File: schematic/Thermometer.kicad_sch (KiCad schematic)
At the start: 17 parts, among them Q1 BC547, Q2 BC547, Q3 BC547, Q4 BC547, SW1 SW_SPDT, U1 CC56-12EWA, U2 DS18B20, U3 DS18B20

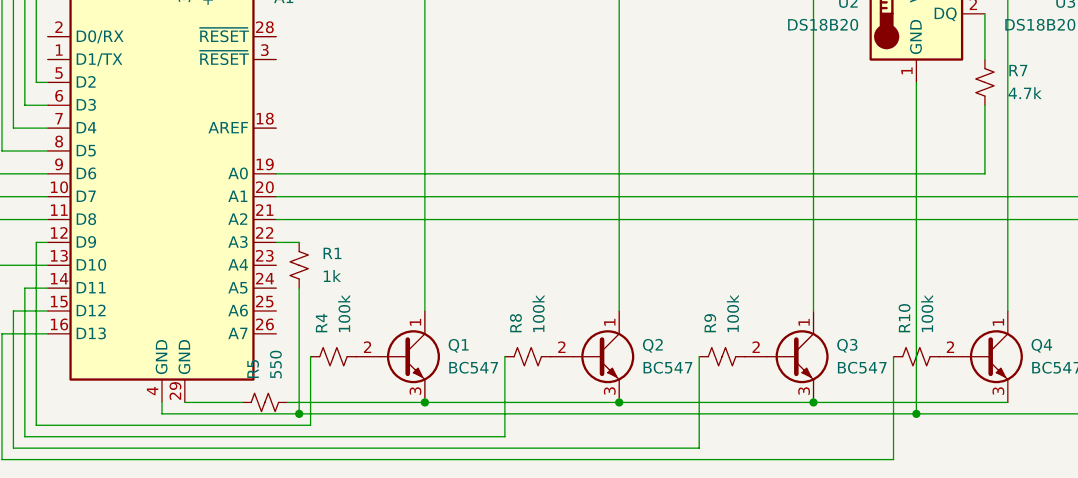
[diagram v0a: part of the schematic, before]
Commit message: Created a PCB design for the board
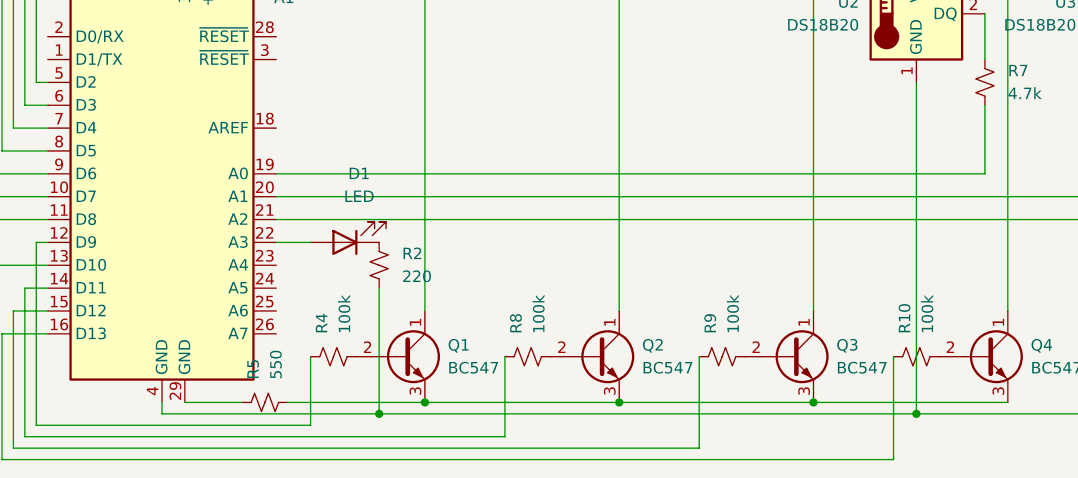
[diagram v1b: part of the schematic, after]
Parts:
- removed R1: 1k, symbol Device:R_Small_US
- added D1: LED, LED_THT:LED_D5.0mm, symbol Device:LED
- added R2: 220, Resistor_THT:R_Axial_DIN0204_L3.6mm_D1.6mm_P5.08mm_Horizontal, symbol Device:R_Small_US
- R10, R4, R5, R6, R7, R8, R9: footprint (none) -> Resistor_THT:R_Axial_DIN0204_L3.6mm_D1.6mm_P5.08mm_Horizontal
- SW1: footprint (none) -> Button_Switch_THT:SW_CK_JS202011CQN_DPDT_Straight
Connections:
- net at A1.4 (GND), SW1.3 (C), U2.1 (GND)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: now also R2.2
- net at A1.22 (A3): now also D1.2 (A)
- new net: D1.1 (K), R2.1
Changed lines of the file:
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@@
 	)
 	(junction
-		(at 54.61 95.25)
+		(at 63.5 95.25)
 		(diameter 0)
 		(color 0 0 0 0)
@@
 	(wire
 		(pts
-			(xy 52.07 76.2) (xy 54.61 76.2)
-		)
-		(stroke
-			(width 0)
-			(type default)
-		)
-	)
-	(wire
-		(pts
 			(xy 26.67 66.04) (xy 21.59 66.04)
 		)
@@
 	(wire
 		(pts
-			(xy 54.61 95.25) (xy 123.19 95.25)
+			(xy 63.5 95.25) (xy 123.19 95.25)
+		)
+		(stroke
+			(width 0)
+			(type default)
+		)
+	)
+	(wire
+		(pts
+			(xy 39.37 95.25) (xy 63.5 95.25)
 		)
 		(stroke
@@
 	(wire
 		(pts
+			(xy 52.07 76.2) (xy 55.88 76.2)
+		)
+		(stroke
+			(width 0)
+			(type default)
+		)
+	)
+	(wire
+		(pts
 			(xy 17.78 36.83) (xy 26.67 36.83)
 		)
@@
 	(wire
 		(pts
-			(xy 54.61 81.28) (xy 54.61 95.25)
-		)
-		(stroke
-			(width 0)
-			(type default)
-		)
-	)
-	(wire
-		(pts
-			(xy 39.37 95.25) (xy 54.61 95.25)
-		)
-		(stroke
-			(width 0)
-			(type default)
-		)
-	)
-	(wire
-		(pts
 			(xy 111.76 93.98) (xy 133.35 93.98)
 		)
@@
 		(pts
 			(xy 20.32 31.75) (xy 26.67 31.75)
+		)
+		(stroke
+			(width 0)
+			(type default)
+		)
+	)
+	(wire
+		(pts
+			(xy 63.5 81.28) (xy 63.5 95.25)
 		)
 		(stroke
@@
 			)
 		)
-		(property "Footprint" ""
+		(property "Footprint" "Resistor_THT:R_Axial_DIN0204_L3.6mm_D1.6mm_P5.08mm_Horizontal"
 			(at 80.01 88.9 0)
 			(effects
@@
 			)
 		)
-		(property "Footprint" ""
+		(property "Footprint" "Resistor_THT:R_Axial_DIN0204_L3.6mm_D1.6mm_P5.08mm_Horizontal"
 			(at 154.94 58.42 0)
 			(effects
@@
 			)
 		)
-		(property "Footprint" ""
+		(property "Footprint" "Resistor_THT:R_Axial_DIN0204_L3.6mm_D1.6mm_P5.08mm_Horizontal"
 			(at 130.81 58.42 0)
 			(effects
@@
 	(symbol
 		(lib_id "Device:R_Small_US")
+		(at 63.5 78.74 0)
+		(unit 1)
+		(exclude_from_sim no)
+		(in_bom yes)
+		(on_board yes)
+		(dnp no)
+		(fields_autoplaced yes)
+		(property "Reference" "R2"
+			(at 66.04 77.4699 0)
+			(effects
+				(font
+					(size 1.27 1.27)
+				)
+				(justify left)
+			)
+		)
+		(property "Value" "220"
+			(at 66.04 80.0099 0)
+			(effects
+				(font
+					(size 1.27 1.27)
+				)
+				(justify left)
+			)
+		)
+		(property "Footprint" "Resistor_THT:R_Axial_DIN0204_L3.6mm_D1.6mm_P5.08mm_Horizontal"
+			(at 63.5 78.74 0)
+			(effects
+				(font
+					(size 1.27 1.27)
+				)
+				(hide yes)
+			)
+		)
+		(property "Datasheet" "~"
+			(at 63.5 78.74 0)
+			(effects
+				(font
+					(size 1.27 1.27)
+				)
+				(hide yes)
+			)
+		)
+		(property "Description" "Resistor, small US symbol"
+			(at 63.5 78.74 0)
+			(effects
+				(font
+					(size 1.27 1.27)
+				)
+				(hide yes)
+			)
+		)
+		(pin "2"
+		)
+		(pin "1"
+		)
+		(instances
+			(project ""
+				(path "/81b9514e-2b12-47cb-ad97-5183a669bf2a"
+					(reference "R2")
+					(unit 1)
+				)
+			)
+		)
+	)
+	(symbol
+		(lib_id "Device:LED")
+		(at 59.69 76.2 180)
+		(unit 1)
+		(exclude_from_sim no)
+		(in_bom yes)
+		(on_board yes)
+		(dnp no)
+		(fields_autoplaced yes)
+		(property "Reference" "D1"
+			(at 61.2775 68.58 0)
+			(effects
+				(font
+					(size 1.27 1.27)
+				)
+			)
+		)
+		(property "Value" "LED"
+			(at 61.2775 71.12 0)
+			(effects
+				(font
+					(size 1.27 1.27)
+				)
+			)
+		)
+		(property "Footprint" "LED_THT:LED_D5.0mm"
+			(at 59.69 76.2 0)
+			(effects
+				(font
+					(size 1.27 1.27)
+				)
+				(hide yes)
+			)
+		)
+		(property "Datasheet" "~"
+			(at 59.69 76.2 0)
+			(effects
+				(font
+					(size 1.27 1.27)
+				)
+				(hide yes)
+			)
+		)
+		(property "Description" "Light emitting diode"
+			(at 59.69 76.2 0)
+			(effects
+				(font
+					(size 1.27 1.27)
+				)
+				(hide yes)
+			)
+		)
+		(property "Sim.Pins" "1=K 2=A"
+			(at 59.69 76.2 0)
+			(effects
+				(font
+					(size 1.27 1.27)
+				)
+				(hide yes)
+			)
+		)
+		(pin "1"
+		)
+		(pin "2"
+		)
+		(instances
+			(project ""
+				(path "/81b9514e-2b12-47cb-ad97-5183a669bf2a"
+					(reference "D1")
+					(unit 1)
+				)
+			)
+		)
+	)
+	(symbol
+		(lib_id "Device:R_Small_US")
 		(at 101.6 88.9 90)
 		(unit 1)
@@
 			)
 		)
-		(property "Footprint" ""
+		(property "Footprint" "Resistor_THT:R_Axial_DIN0204_L3.6mm_D1.6mm_P5.08mm_Horizontal"
 			(at 101.6 88.9 0)
 			(effects
@@
 	)
 	(symbol
-		(lib_id "Device:R_Small_US")
-		(at 54.61 78.74 0)
-		(unit 1)
-		(exclude_from_sim no)
-		(in_bom yes)
-		(on_board yes)
-		(dnp no)
-		(fields_autoplaced yes)
-		(property "Reference" "R1"
-			(at 57.15 77.4699 0)
-			(effects
-				(font
-					(size 1.27 1.27)
-				)
-				(justify left)
-			)
-		)
-		(property "Value" "1k"
-			(at 57.15 80.0099 0)
-			(effects
-				(font
-					(size 1.27 1.27)
-				)
-				(justify left)
-			)
-		)
-		(property "Footprint" ""
-			(at 54.61 78.74 0)
-			(effects
-				(font
-					(size 1.27 1.27)
-				)
-				(hide yes)
-			)
-		)
-		(property "Datasheet" "~"
-			(at 54.61 78.74 0)
-			(effects
-				(font
-					(size 1.27 1.27)
-				)
-				(hide yes)
-			)
-		)
-		(property "Description" "Resistor, small US symbol"
-			(at 54.61 78.74 0)
-			(effects
-				(font
-					(size 1.27 1.27)
-				)
-				(hide yes)
-			)
-		)
-		(pin "1"
-		)
-		(pin "2"
-		)
-		(instances
-			(project ""
-				(path "/81b9514e-2b12-47cb-ad97-5183a669bf2a"
-					(reference "R1")
-					(unit 1)
-				)
-			)
-		)
-	)
-	(symbol
 		(lib_id "Transistor_BJT:BC547")
 		(at 87.63 88.9 0)
@@
 			)
 		)
-		(property "Footprint" ""
+		(property "Footprint" "Resistor_THT:R_Axial_DIN0204_L3.6mm_D1.6mm_P5.08mm_Horizontal"
 			(at 58.42 88.9 0)
 			(effects
@@
 			)
 		)
-		(property "Footprint" ""
+		(property "Footprint" "Button_Switch_THT:SW_CK_JS202011CQN_DPDT_Straight"
 			(at 147.32 88.9 0)
 			(effects
@@
 			)
 		)
-		(property "Footprint" ""
+		(property "Footprint" "Resistor_THT:R_Axial_DIN0204_L3.6mm_D1.6mm_P5.08mm_Horizontal"
 			(at 50.8 93.98 0)
 			(effects
@@
 			)
 		)
-		(property "Footprint" ""
+		(property "Footprint" "Resistor_THT:R_Axial_DIN0204_L3.6mm_D1.6mm_P5.08mm_Horizontal"
 			(at 123.19 88.9 0)
 			(effects

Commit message: Updated Schematic and PCB with (hopefully) final designs
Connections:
- net at U2.2 (DQ): now also A1.19 (A0), R7.2; no longer R7.1
- net at A1.27 (+5V), SW1.1 (A), U2.3 (V_{DD})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: now also R6.2, R7.1
- net at R6.1, U3.2 (DQ): now also A1.20 (A1)
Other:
- moved on the sheet: R6, R7
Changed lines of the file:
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@@
+	)
+	(junction
+		(at 160.02 50.8)
+		(diameter 0)
+		(color 0 0 0 0)
 	)
 	(junction
@@
 	)
 	(junction
+		(at 130.81 50.8)
+		(diameter 0)
+		(color 0 0 0 0)
+	)
+	(junction
+		(at 154.94 50.8)
+		(diameter 0)
+		(color 0 0 0 0)
+	)
+	(junction
+		(at 130.81 43.18)
+		(diameter 0)
+		(color 0 0 0 0)
+	)
+	(junction
 		(at 147.32 43.18)
 		(diameter 0)
@@
 	(wire
 		(pts
-			(xy 147.32 43.18) (xy 163.83 43.18)
+			(xy 147.32 43.18) (xy 160.02 43.18)
 		)
 		(stroke
@@
 	(wire
 		(pts
+			(xy 160.02 50.8) (xy 160.02 93.98)
+		)
+		(stroke
+			(width 0)
+			(type default)
+		)
+	)
+	(wire
+		(pts
 			(xy 26.67 66.04) (xy 21.59 66.04)
 		)
@@
 	(wire
 		(pts
-			(xy 130.81 60.96) (xy 130.81 68.58)
-		)
-		(stroke
-			(width 0)
-			(type default)
-		)
-	)
-	(wire
-		(pts
 			(xy 25.4 96.52) (xy 25.4 76.2)
 		)
@@
 	(wire
 		(pts
-			(xy 123.19 43.18) (xy 147.32 43.18)
+			(xy 123.19 43.18) (xy 130.81 43.18)
 		)
 		(stroke
@@
 	(wire
 		(pts
-			(xy 154.94 60.96) (xy 154.94 71.12)
-		)
-		(stroke
-			(width 0)
-			(type default)
-		)
-	)
-	(wire
-		(pts
 			(xy 41.91 93.98) (xy 48.26 93.98)
 		)
@@
 	(wire
 		(pts
+			(xy 130.81 43.18) (xy 147.32 43.18)
+		)
+		(stroke
+			(width 0)
+			(type default)
+		)
+	)
+	(wire
+		(pts
 			(xy 26.67 71.12) (xy 19.05 71.12)
 		)
@@
 	(wire
 		(pts
-			(xy 130.81 50.8) (xy 130.81 55.88)
+			(xy 130.81 50.8) (xy 130.81 68.58)
 		)
 		(stroke
@@
 	(wire
 		(pts
-			(xy 163.83 93.98) (xy 149.86 93.98)
+			(xy 160.02 93.98) (xy 149.86 93.98)
 		)
 		(stroke
@@
 	(wire
 		(pts
+			(xy 130.81 43.18) (xy 130.81 45.72)
+		)
+		(stroke
+			(width 0)
+			(type default)
+		)
+	)
+	(wire
+		(pts
 			(xy 111.76 93.98) (xy 133.35 93.98)
 		)
@@
 	(wire
 		(pts
-			(xy 163.83 43.18) (xy 163.83 93.98)
+			(xy 160.02 43.18) (xy 160.02 50.8)
 		)
 		(stroke
@@
 	(wire
 		(pts
-			(xy 154.94 50.8) (xy 154.94 55.88)
+			(xy 154.94 50.8) (xy 154.94 71.12)
 		)
 		(stroke
@@
 	(symbol
 		(lib_id "Device:R_Small_US")
-		(at 154.94 58.42 0)
+		(at 157.48 50.8 90)
 		(unit 1)
 		(exclude_from_sim no)
@@
 		(fields_autoplaced yes)
 		(property "Reference" "R6"
-			(at 157.48 57.1499 0)
-			(effects
-				(font
-					(size 1.27 1.27)
-				)
-				(justify left)
+			(at 157.48 44.45 90)
+			(effects
+				(font
+					(size 1.27 1.27)
+				)
 			)
 		)
 		(property "Value" "4.7k"
-			(at 157.48 59.6899 0)
-			(effects
-				(font
-					(size 1.27 1.27)
-				)
-				(justify left)
+			(at 157.48 46.99 90)
+			(effects
+				(font
+					(size 1.27 1.27)
+				)
 			)
 		)
 		(property "Footprint" "Resistor_THT:R_Axial_DIN0204_L3.6mm_D1.6mm_P5.08mm_Horizontal"
-			(at 154.94 58.42 0)
+			(at 157.48 50.8 0)
 			(effects
 				(font
@@
 		)
 		(property "Datasheet" "~"
-			(at 154.94 58.42 0)
+			(at 157.48 50.8 0)
 			(effects
 				(font
@@
 		)
 		(property "Description" "Resistor, small US symbol"
-			(at 154.94 58.42 0)
+			(at 157.48 50.8 0)
 			(effects
 				(font
@@
 	(symbol
 		(lib_id "Device:R_Small_US")
-		(at 130.81 58.42 0)
+		(at 130.81 48.26 0)
 		(unit 1)
 		(exclude_from_sim no)
@@
 		(fields_autoplaced yes)
 		(property "Reference" "R7"
-			(at 133.35 57.1499 0)
+			(at 133.35 46.9899 0)
 			(effects
 				(font
@@
 		)
 		(property "Value" "4.7k"
-			(at 133.35 59.6899 0)
+			(at 133.35 49.5299 0)
 			(effects
 				(font
@@
 		)
 		(property "Footprint" "Resistor_THT:R_Axial_DIN0204_L3.6mm_D1.6mm_P5.08mm_Horizontal"
-			(at 130.81 58.42 0)
+			(at 130.81 48.26 0)
 			(effects
 				(font
@@
 		)
 		(property "Datasheet" "~"
-			(at 130.81 58.42 0)
+			(at 130.81 48.26 0)
 			(effects
 				(font
@@
 		)
 		(property "Description" "Resistor, small US symbol"
-			(at 130.81 58.42 0)
-			(effects
-				(font
+			(at 130.81 48.26 0)
+			(effects
+				(font
